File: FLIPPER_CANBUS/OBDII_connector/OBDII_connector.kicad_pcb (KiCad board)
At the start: 2 copper layers, 40 x 17 mm, 4 parts, among them J1 Conn_02x08_Counter_Clockwise, J2 Conn_01x02

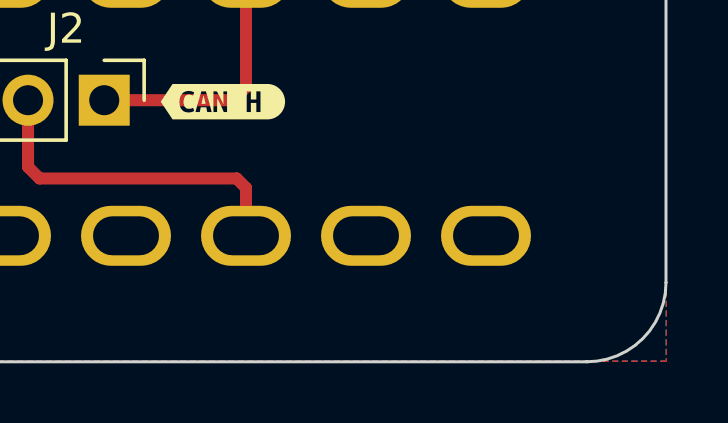
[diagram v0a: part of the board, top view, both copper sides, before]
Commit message: feat: version Label got updated
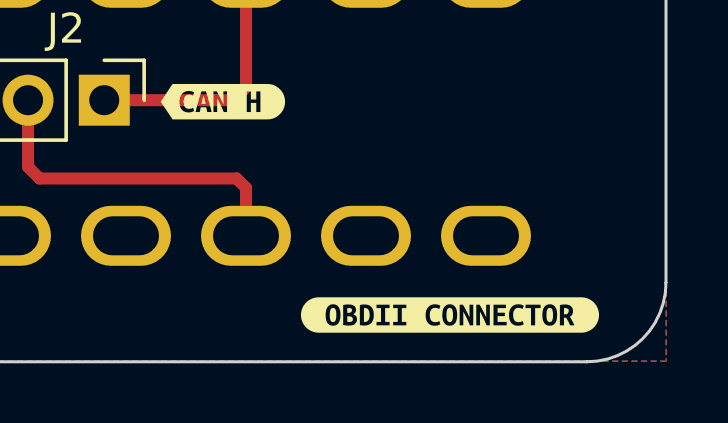
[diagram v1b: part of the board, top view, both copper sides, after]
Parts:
- added kibuzzard-66706F79: G***, kibuzzard-66706F79, F.Cu at (127.7, 68.2)

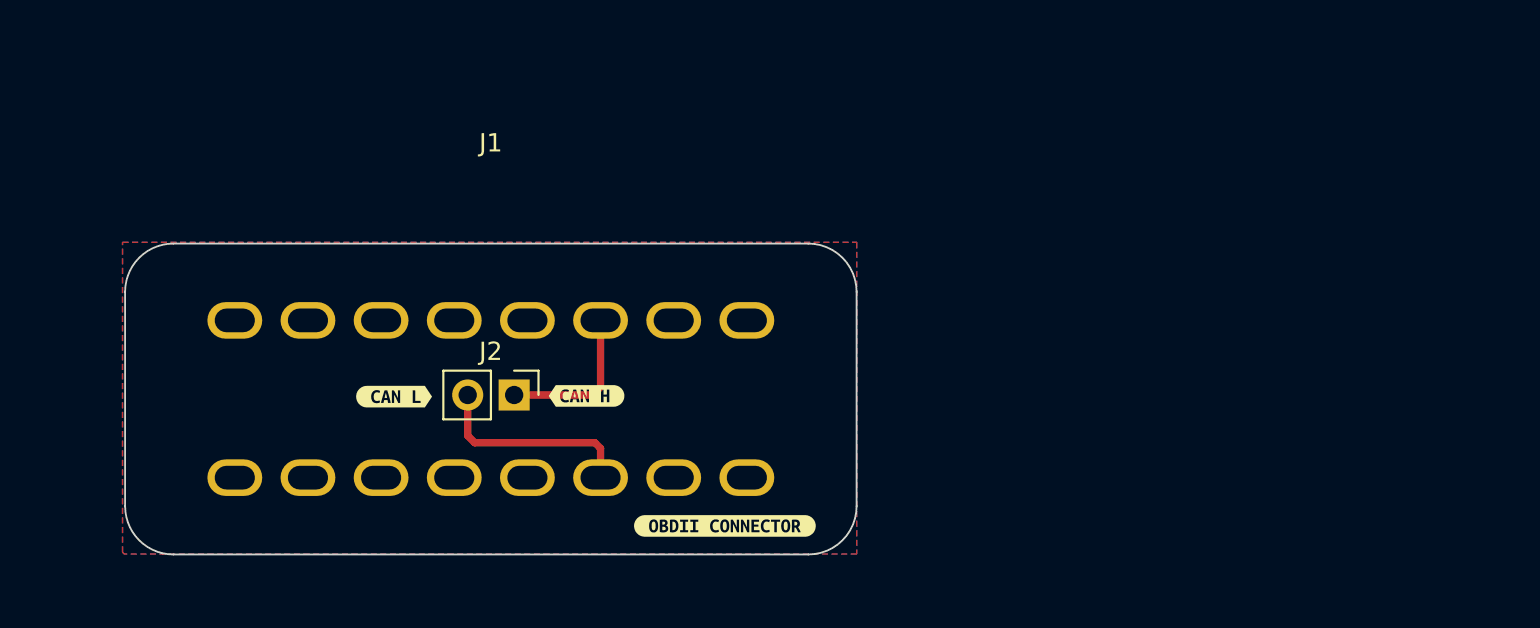
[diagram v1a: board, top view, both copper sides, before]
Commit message: feat: change shape of PCB & indicators added
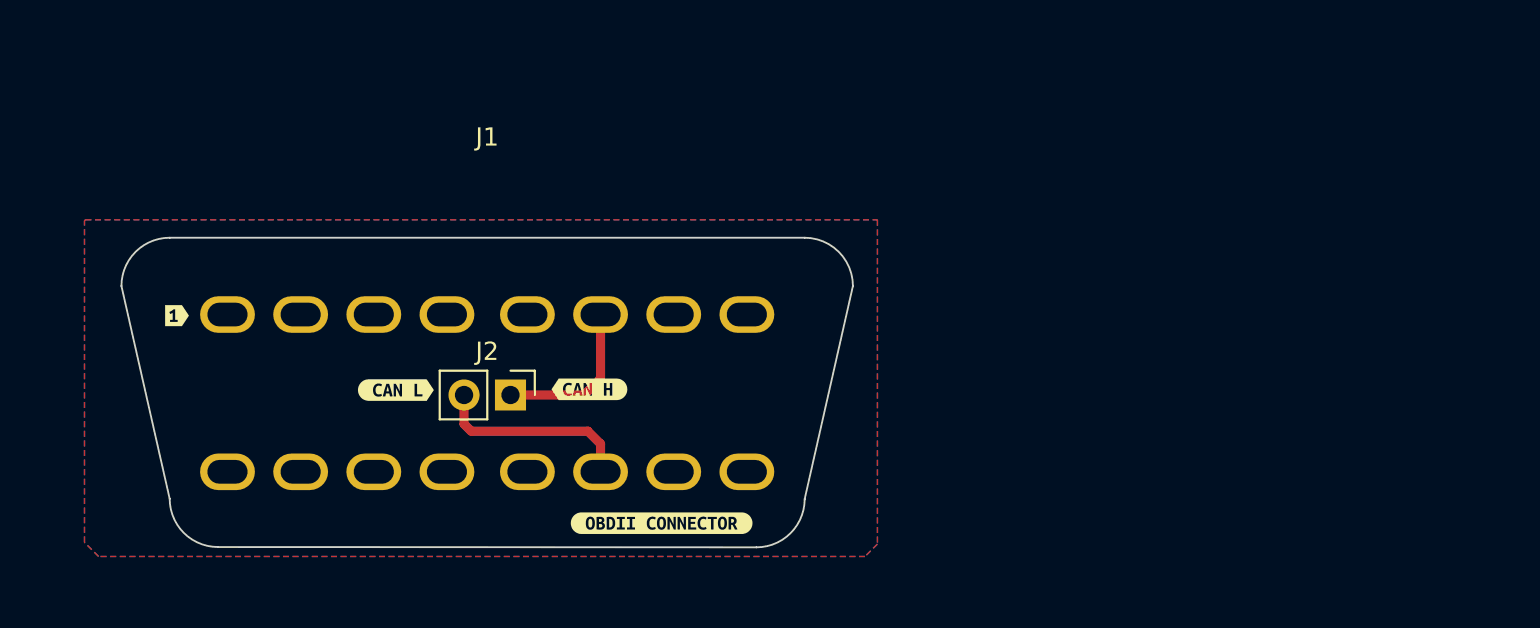
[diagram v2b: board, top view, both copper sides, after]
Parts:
- added kibuzzard-66732750: G***, kibuzzard-66732750, F.Cu at (97.7, 56.7)
- moved kibuzzard-66706F79 3.46 mm to (124.2, 68.1)
- moved kibuzzard-6646749E 0.39 mm to (120.3, 60.8)
- moved J1 0.38 mm to (114.7, 47.5)
- moved kibuzzard-66467618 0.37 mm to (109.7, 60.8)
- moved J2 0.20 mm to (116.0, 61.1)
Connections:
- J1 pad 4: Earth -> unconnected-(J1-Pin_4-Pad4)
- J1 pad 5: unconnected-(J1-Pin_5-Pad5) -> GND
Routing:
- added copper zone on B.Cu, net GND
- added copper zone on F.Cu, net GND
- removed copper zone on B.Cu, net Earth
- removed copper zone on F.Cu, net Earth
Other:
- board size 40 x 17 mm -> 40 x 16.9 mm

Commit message: feat: position indicator added
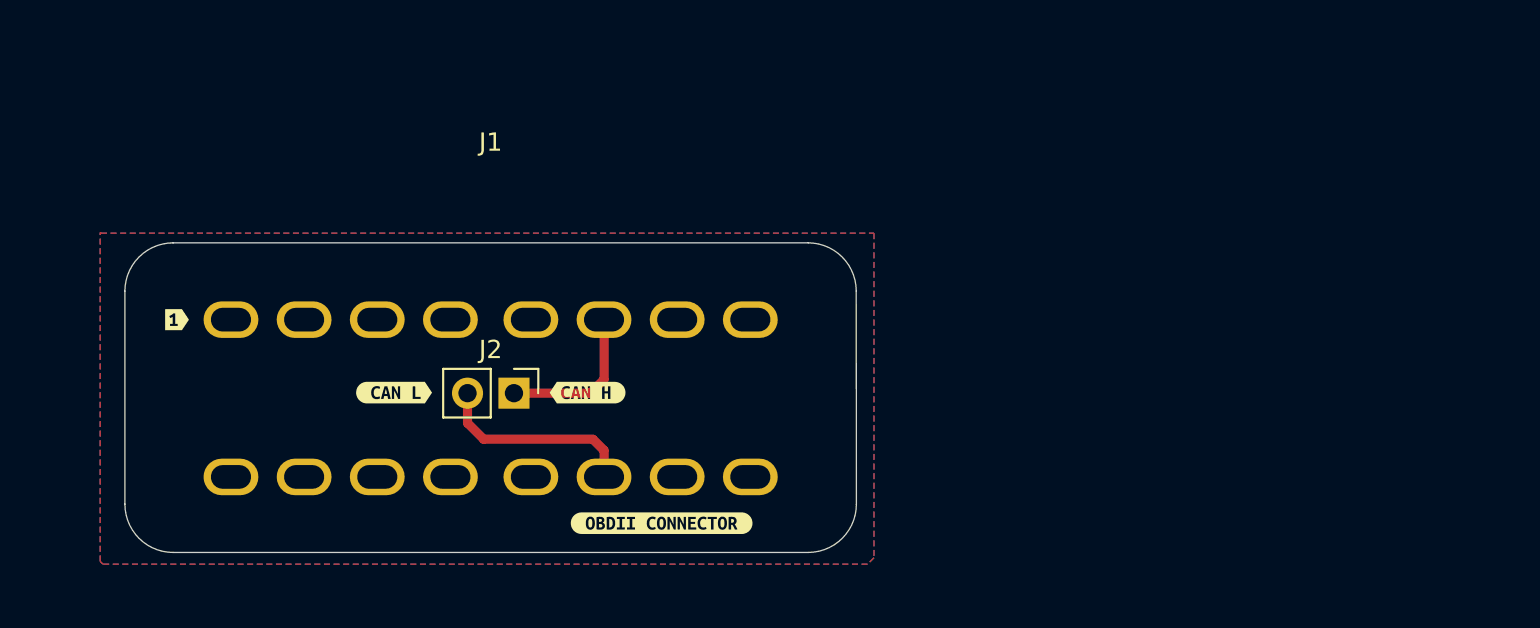
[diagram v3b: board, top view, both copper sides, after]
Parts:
- moved J1 0.34 mm to (114.9, 47.8)
- moved kibuzzard-66732750 0.22 mm to (97.7, 57.0)
- moved J2 0.21 mm to (116.2, 61.0)
- moved kibuzzard-6646749E 0.21 mm to (120.2, 61.0)
- moved kibuzzard-66467618 0.17 mm to (109.6, 61.0)
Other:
- outline, holes or cut-outs redrawn
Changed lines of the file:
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@@
 	(footprint "Connector_PinHeader_2.54mm:PinHeader_1x02_P2.54mm_Vertical"
 		(layer "F.Cu")
-		(at 115.975 61.08 -90)
+		(at 116.165 60.98 -90)
 		(descr "Through hole straight pin header, 1x02, 2.54mm pitch, single row")
 		(tags "Through hole pin header THT 1x02 2.54mm single row")
@@
 	(footprint "Case:OBD-II-Sparkfun"
 		(layer "F.Cu")
-		(at 114.7 47.48)
+		(at 114.89 47.76)
 		(property "Reference" "J1"
 			(at 0 -0.5 0)
@@
 		(attr through_hole)
 		(fp_line
+			(start -17.528061 18.471939)
+			(end -19.038135 8.258072)
+			(stroke
+				(width 0.05)
+				(type default)
+			)
+			(layer "B.SilkS")
+			(net 4928)
+		)
+		(fp_line
+			(start -17.01 6.23)
+			(end -0.01 6.23)
+			(stroke
+				(width 0.05)
+				(type default)
+			)
+			(layer "B.SilkS")
+			(net 4928)
+		)
+		(fp_line
+			(start -15.5 20.5)
+			(end 0 20.5)
+			(stroke
+				(width 0.05)
+				(type default)
+			)
+			(layer "B.SilkS")
+			(net 4928)
+		)
+		(fp_line
+			(start -0.01 6.23)
+			(end 16.99 6.23)
+			(stroke
+				(width 0.05)
+				(type default)
+			)
+			(layer "B.SilkS")
+			(net 4928)
+		)
+		(fp_line
+			(start 0 20.5)
+			(end 15.5 20.5)
+			(stroke
+				(width 0.05)
+				(type default)
+			)
+			(layer "B.SilkS")
+			(net 4928)
+		)
+		(fp_line
+			(start 17.528061 18.471939)
+			(end 19.018061 8.258061)
+			(stroke
+				(width 0.05)
+				(type default)
+			)
+			(layer "B.SilkS")
+			(net 4928)
+		)
+		(fp_arc
+			(start -19.038061 8.258061)
+			(mid -18.444056 6.824005)
+			(end -17.01 6.23)
+			(stroke
+				(width 0.05)
+				(type default)
+			)
+			(layer "B.SilkS")
+			(net 4928)
+		)
+		(fp_arc
+			(start -15.5 20.5)
+			(mid -16.833753 19.805692)
+			(end -17.528061 18.471939)
+			(stroke
+				(width 0.05)
+				(type default)
+			)
+			(layer "B.SilkS")
+			(net 4928)
+		)
+		(fp_arc
+			(start 16.99 6.23)
+			(mid 18.424055 6.824005)
+			(end 19.018061 8.258061)
+			(stroke
+				(width 0.05)
+				(type default)
+			)
+			(layer "B.SilkS")
+			(net 4928)
+		)
+		(fp_arc
+			(start 17.528061 18.471939)
+			(mid 16.833753 19.805692)
+			(end 15.5 20.5)
+			(stroke
+				(width 0.05)
+				(type default)
+			)
+			(layer "B.SilkS")
+			(net 4928)
+		)
+		(fp_line
 			(start -13.695496 12.603992)
 			(end 13.705953 12.597845)
@@
 		)
 		(fp_line
-			(start -17.361522 5)
-			(end 17.361522 5)
-			(stroke
-				(width 0.1)
+			(start -20 7.64)
+			(end -20 19.29)
+			(stroke
+				(width 0.05)
 				(type default)
 			)
@@
 		)
 		(fp_line
-			(start -17.361522 19.274314)
-			(end -20 7.638478)
-			(stroke
-				(width 0.1)
+			(start -17.36 5)
+			(end 17.36 5)
+			(stroke
+				(width 0.05)
 				(type default)
 			)
@@
 		)
 		(fp_line
-			(start -14.723044 21.912792)
-			(end 14.723044 21.929998)
-			(stroke
-				(width 0.1)
+			(start 17.36 21.93)
+			(end -17.36 21.93)
+			(stroke
+				(width 0.05)
 				(type default)
 			)
@@
 		)
 		(fp_line
-			(start 17.361522 19.29152)
-			(end 20 7.638478)
-			(stroke
-				(width 0.1)
+			(start 19.99 7.63)
+			(end 20 19.29)
+			(stroke
+				(width 0.05)
 				(type default)
 			)
@@
 		)
 		(fp_arc
-			(start -20 7.638478)
-			(mid -19.227208 5.772792)
-			(end -17.361522 5)
-			(stroke
-				(width 0.1)
+			(start -20 7.64)
+			(mid -19.226762 5.773238)
+			(end -17.36 5)
+			(stroke
+				(width 0.05)
 				(type default)
 			)
@@
 		)
 		(fp_arc
-			(start -14.723044 21.912792)
-			(mid -16.58873 21.14)
-			(end -17.361522 19.274314)
-			(stroke
-				(width 0.1)
+			(start -17.36 21.93)
+			(mid -19.226762 21.156762)
+			(end -20 19.29)
+			(stroke
+				(width 0.05)
 				(type default)
 			)
@@
 		)
 		(fp_arc
-			(start 17.361522 5)
-			(mid 19.227201 5.772799)
-			(end 20 7.638478)
-			(stroke
-				(width 0.1)
+			(start 17.36 5)
+			(mid 19.219691 5.770309)
+			(end 19.99 7.63)
+			(stroke
+				(width 0.05)
 				(type default)
 			)
@@
 		)
 		(fp_arc
-			(start 17.361522 19.29152)
-			(mid 16.58873 21.157207)
-			(end 14.723044 21.929998)
-			(stroke
-				(width 0.1)
+			(start 20 19.29)
+			(mid 19.226762 21.156762)
+			(end 17.36 21.93)
+			(stroke
+				(width 0.05)
 				(type default)
 			)
@@
 	(footprint "kibuzzard-66467618"
 		(layer "F.Cu")
-		(at 109.71 60.81)
+		(at 109.61 60.95)
 		(descr "Generated with KiBuzzard")
 		(tags "kb_params=eyJBbGlnbm1lbnRDaG9pY2UiOiAiQ2VudGVyIiwgIkNhcExlZnRDaG9pY2UiOiAiKCIsICJDYXBSaWdodENob2ljZSI6ICI+IiwgIkZvbnRDb21ib0JveCI6ICJVYnVudHVNb25vLUIiLCAiSGVpZ2h0Q3RybCI6ICIuNyIsICJMYXllckNvbWJvQm94IjogIkYuU2lsa1MiLCAiTXVsdGlMaW5lVGV4dCI6ICJDQU4gTCIsICJQYWRkaW5nQm90dG9tQ3RybCI6ICI1IiwgIlBhZGRpbmdMZWZ0Q3RybCI6ICI1IiwgIlBhZGRpbmdSaWdodEN0cmwiOiAiNSIsICJQYWRkaW5nVG9wQ3RybCI6ICI1IiwgIldpZHRoQ3RybCI6ICIifQ==")
@@
 	(footprint "kibuzzard-6646749E"
 		(layer "F.Cu")
-		(at 120.29 60.77)
+		(at 120.19 60.95)
 		(descr "Generated with KiBuzzard")
 		(tags "kb_params=eyJBbGlnbm1lbnRDaG9pY2UiOiAiQ2VudGVyIiwgIkNhcExlZnRDaG9pY2UiOiAiPCIsICJDYXBSaWdodENob2ljZSI6ICIpIiwgIkZvbnRDb21ib0JveCI6ICJVYnVudHVNb25vLUIiLCAiSGVpZ2h0Q3RybCI6ICIuNyIsICJMYXllckNvbWJvQm94IjogIkYuU2lsa1MiLCAiTXVsdGlMaW5lVGV4dCI6ICJDQU4gSCIsICJQYWRkaW5nQm90dG9tQ3RybCI6ICI1IiwgIlBhZGRpbmdMZWZ0Q3RybCI6ICI1IiwgIlBhZGRpbmdSaWdodEN0cmwiOiAiNSIsICJQYWRkaW5nVG9wQ3RybCI6ICI1IiwgIldpZHRoQ3RybCI6ICIifQ==")
@@
 	(footprint "kibuzzard-66732750"
 		(layer "F.Cu")
-		(at 97.74 56.74)
+		(at 97.74 56.96)
 		(descr "Generated with KiBuzzard")
 		(tags "kb_params=eyJBbGlnbm1lbnRDaG9pY2UiOiAiQ2VudGVyIiwgIkNhcExlZnRDaG9pY2UiOiAiWyIsICJDYXBSaWdodENob2ljZSI6ICI+IiwgIkZvbnRDb21ib0JveCI6ICJVYnVudHVNb25vLUIiLCAiSGVpZ2h0Q3RybCI6ICIuNyIsICJMYXllckNvbWJvQm94IjogIkYuU2lsa1MiLCAiTXVsdGlMaW5lVGV4dCI6ICIxIiwgIlBhZGRpbmdCb3R0b21DdHJsIjogIjUiLCAiUGFkZGluZ0xlZnRDdHJsIjogIjUiLCAiUGFkZGluZ1JpZ2h0Q3RybCI6ICI1IiwgIlBhZGRpbmdUb3BDdHJsIjogIjUiLCAiV2lkdGhDdHJsIjogIiJ9")
@@
 	)
 	(segment
-		(start 120.9 60.18)
-		(end 120 61.08)
+		(start 121.09 60.23)
+		(end 120.34 60.98)
 		(width 0.5)
 		(layer "F.Cu")
@@
 	)
 	(segment
-		(start 120 61.08)
-		(end 115.975 61.08)
+		(start 121.09 56.96)
+		(end 121.09 60.23)
 		(width 0.5)
 		(layer "F.Cu")
@@
 	)
 	(segment
-		(start 120.9 56.68)
-		(end 120.9 60.18)
+		(start 120.34 60.98)
+		(end 116.165 60.98)
 		(width 0.5)
 		(layer "F.Cu")
@@
 	)
 	(segment
-		(start 120.21 63.06)
-		(end 120.9 63.75)
+		(start 114.51 63.5)
+		(end 120.48 63.5)
 		(width 0.5)
 		(layer "F.Cu")
@@
 	)
 	(segment
-		(start 113.435 62.665)
-		(end 113.83 63.06)
+		(start 121.09 64.11)
+		(end 121.09 65.56)
 		(width 0.5)
 		(layer "F.Cu")
@@
 	)
 	(segment
-		(start 113.435 61.08)
-		(end 113.435 62.665)
+		(start 113.625 62.615)
+		(end 114.51 63.5)
 		(width 0.5)
 		(layer "F.Cu")
@@
 	)
 	(segment
-		(start 120.9 63.75)
-		(end 120.9 65.28)
+		(start 120.48 63.5)
+		(end 121.09 64.11)
 		(width 0.5)
 		(layer "F.Cu")
@@
 	)
 	(segment
-		(start 113.83 63.06)
-		(end 120.21 63.06)
+		(start 113.625 60.98)
+		(end 113.625 62.615)
 		(width 0.5)
 		(layer "F.Cu")
@@
 		(polygon
 			(pts
-				(xy 92.73 51.5) (xy 136.04 51.5) (xy 136.04 69.23) (xy 135.36 69.91) (xy 93.45 69.91) (xy 92.68 69.14)
-				(xy 92.68 51.55)
-			)
-		)
+				(xy 93.58 52.23) (xy 135.85 52.23) (xy 135.85 69.98) (xy 135.5 70.33) (xy 93.69 70.33) (xy 93.54 70.18)
+				(xy 93.54 52.19)
+			)
+		)

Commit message: fix: space between paths fixed
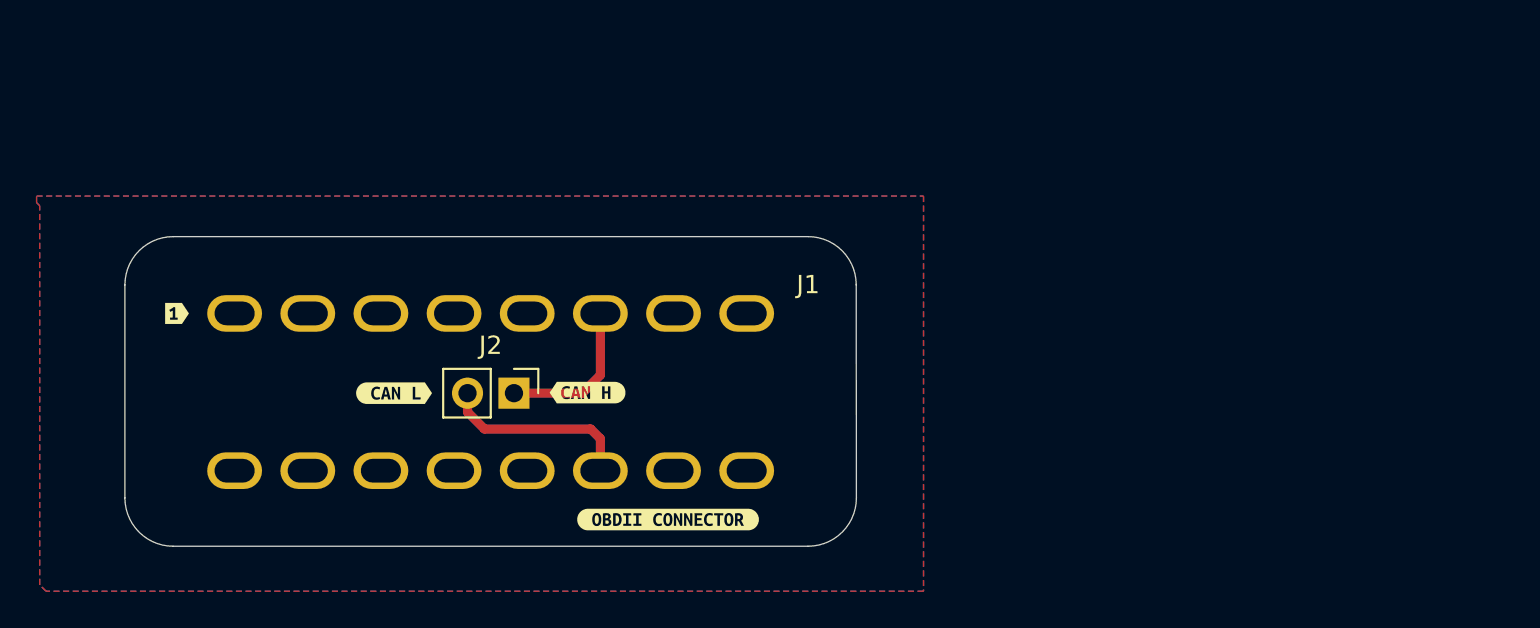
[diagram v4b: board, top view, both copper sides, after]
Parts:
- moved J1 12.9 mm to (114.9, 60.7)
- moved kibuzzard-66706F79 0.40 mm to (124.6, 67.9)
- moved kibuzzard-66732750 0.34 mm to (97.7, 56.6)
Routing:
- net /CAN_L: track 11.2 -> 10.7 mm

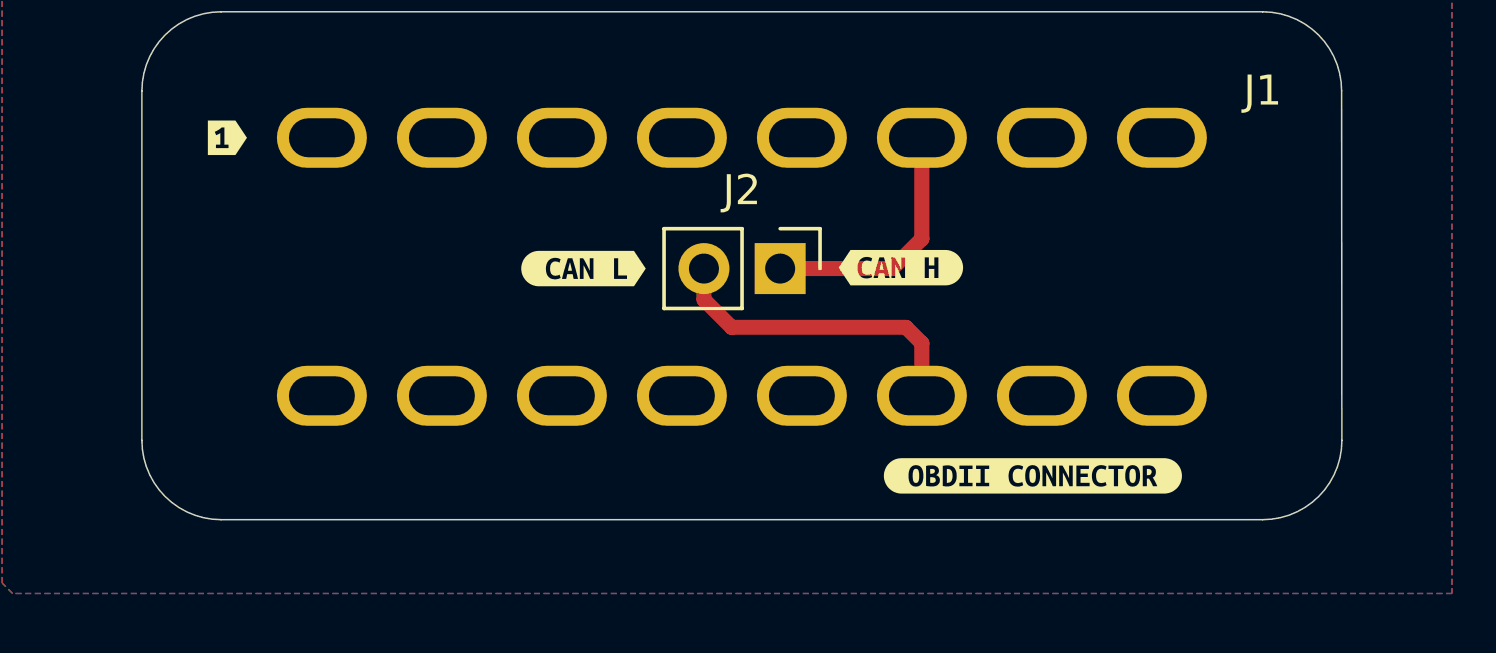
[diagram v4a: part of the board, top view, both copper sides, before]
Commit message: feat(hw): add logos
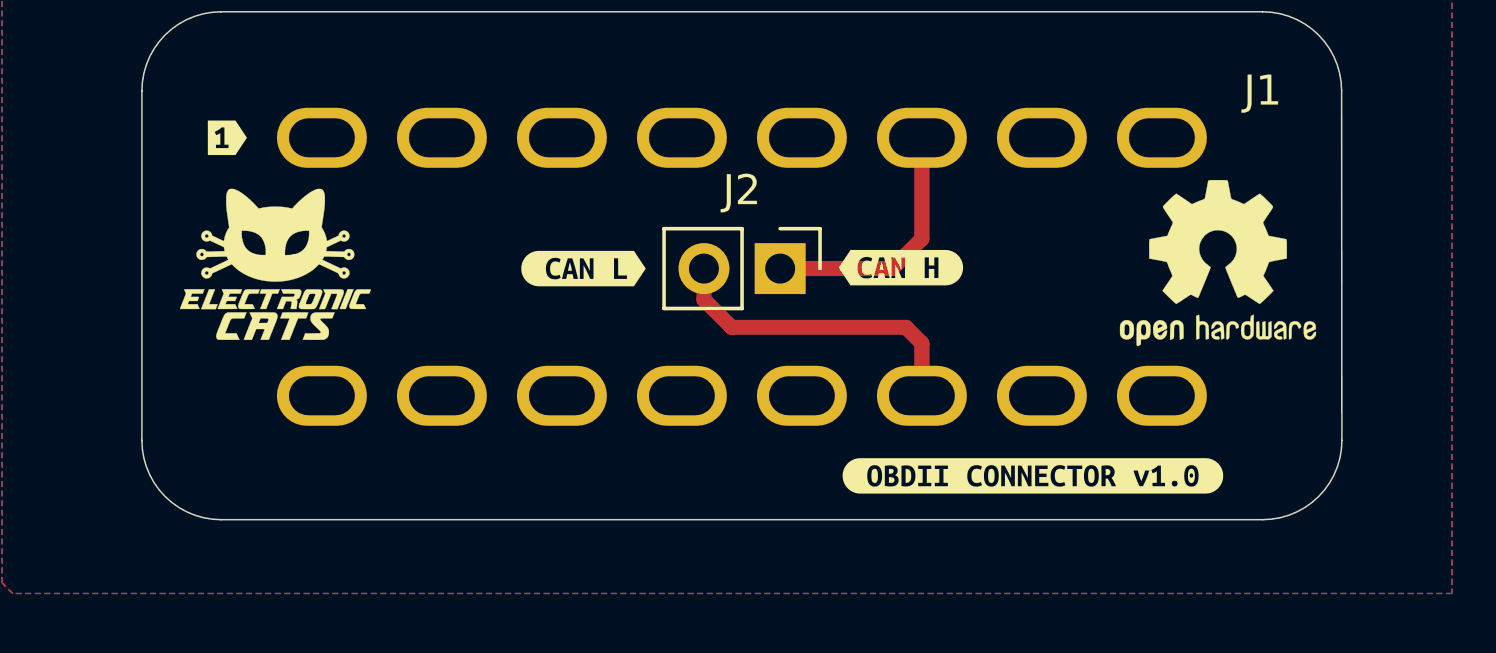
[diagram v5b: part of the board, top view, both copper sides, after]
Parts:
- removed kibuzzard-66706F79: G***, kibuzzard-66706F79
- added G***: LOGO, Aesthetics:electronic_cats_logo_4x3, F.Cu at (99.3, 60.8)
- added G***: LOGO, Aesthetics:electronic_cats_logo_4x3, B.Cu at (130.6, 60.9)
- added REF**: OSHW-Logo2_7.3x6mm_SilkScreen, Symbol:OSHW-Logo2_7.3x6mm_SilkScreen, F.Cu at (130.8, 60.8)
- added kibuzzard-667996B6: G***, kibuzzard-667996B6, F.Cu at (124.6, 67.9)
